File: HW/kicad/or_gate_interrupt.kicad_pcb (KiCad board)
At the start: 2 copper layers, 8 parts, among them P1 CONN_01X06, P2 CONN_01X03, U1 74LS32, U2 74HC02

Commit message: Added a few parts.
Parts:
- added P3: CONN_01X02, Pin_Headers:Pin_Header_Straight_1x02, F.Cu at (130.8, 120.7)
- added U3: ESP-01v090, ESP8266:ESP-01, F.Cu at (121.9, 96.5)
- P2: value CONN_01X03 -> CONN_01X02
- moved R2 7.41 mm to (114.3, 113.0)
- moved P2 7.18 mm to (114.3, 120.7)
- moved P1 5.68 mm to (114.3, 96.5), turned to 180 degrees
- moved R1 5.68 mm to (114.3, 102.9)
- moved R4 3.59 mm to (132.1, 102.9)
- moved U2 2.84 mm to (123.2, 111.8)
- moved R3 2.54 mm to (132.1, 113.0)
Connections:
- P2 pad 1: Net-(P2-Pad1) -> GND
- P2 pad 3: Net-(P1-Pad5) -> (no net)
- R1 pad 2: Net-(P2-Pad1) -> Net-(P2-Pad2)
- U1 pad 1: Net-(P2-Pad1) -> Net-(P2-Pad2)
- U2 pad 1: Net-(P2-Pad2) -> Net-(U2-Pad1)

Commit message: Updated a few layout things.
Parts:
- added C1: CP, Capacitors_ThroughHole:C_Radial_D6.3_L11.2_P2.5, F.Cu at (118.1, 94.0)
- added U4: LT1129CST-3.3, SOT-223, F.Cu at (116.8, 85.1)
- P2: footprint Pin_Headers:Pin_Header_Straight_1x03 -> Pin_Headers:Pin_Header_Straight_1x02
- moved P3 48.4 mm to (119.4, 73.7), turned to 0 degrees
- moved P2 44.5 mm to (114.3, 76.2), turned to 180 degrees
- moved P1 20.9 mm to (134.6, 101.6), turned to 0 degrees
- moved U3 4.02 mm to (125.7, 95.2)
- moved R3 2.54 mm to (129.5, 113.0)
- moved R4 2.54 mm to (129.5, 102.9)
- moved U2 1.80 mm to (121.9, 113.0)
- moved U1 1.27 mm to (121.9, 102.9)
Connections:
- P1 pad 6: +3V3 -> Net-(P1-Pad6)

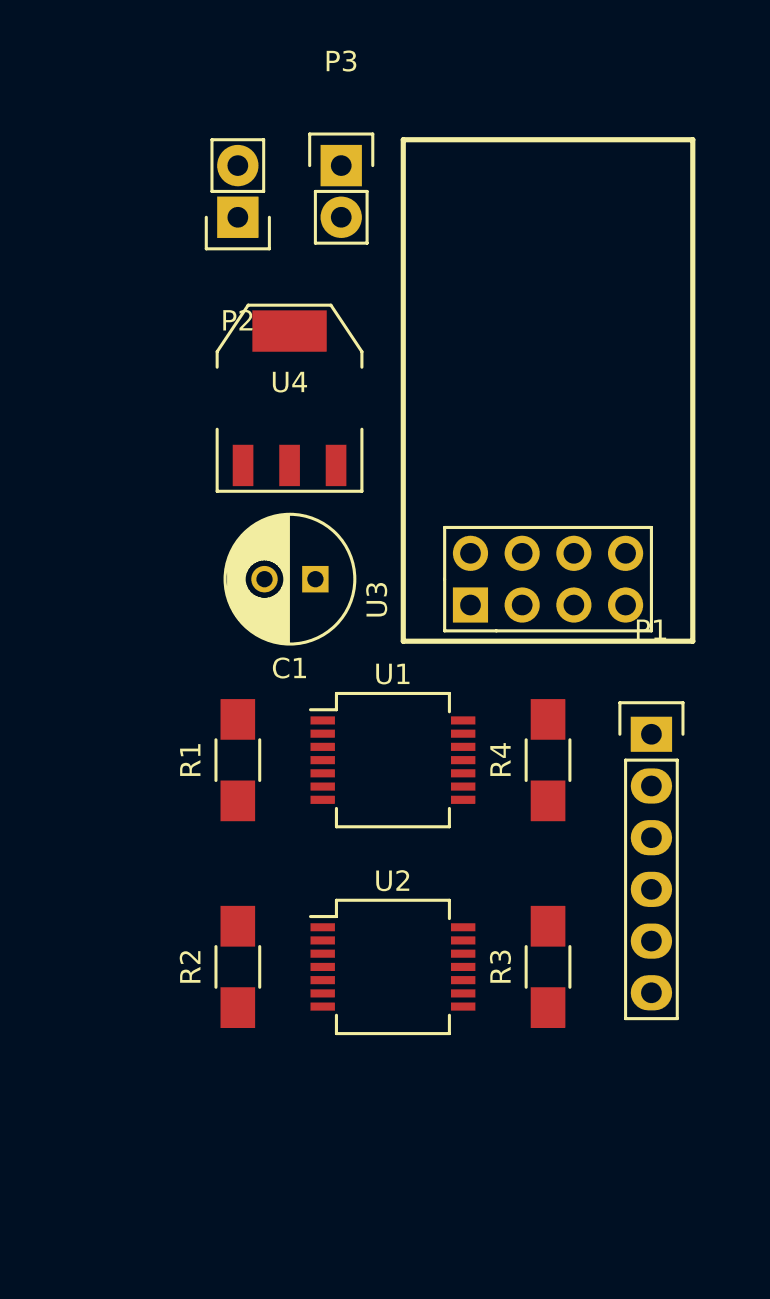
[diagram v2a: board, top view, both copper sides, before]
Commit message: Most of the routing done.  Trying to figure out ground plane.
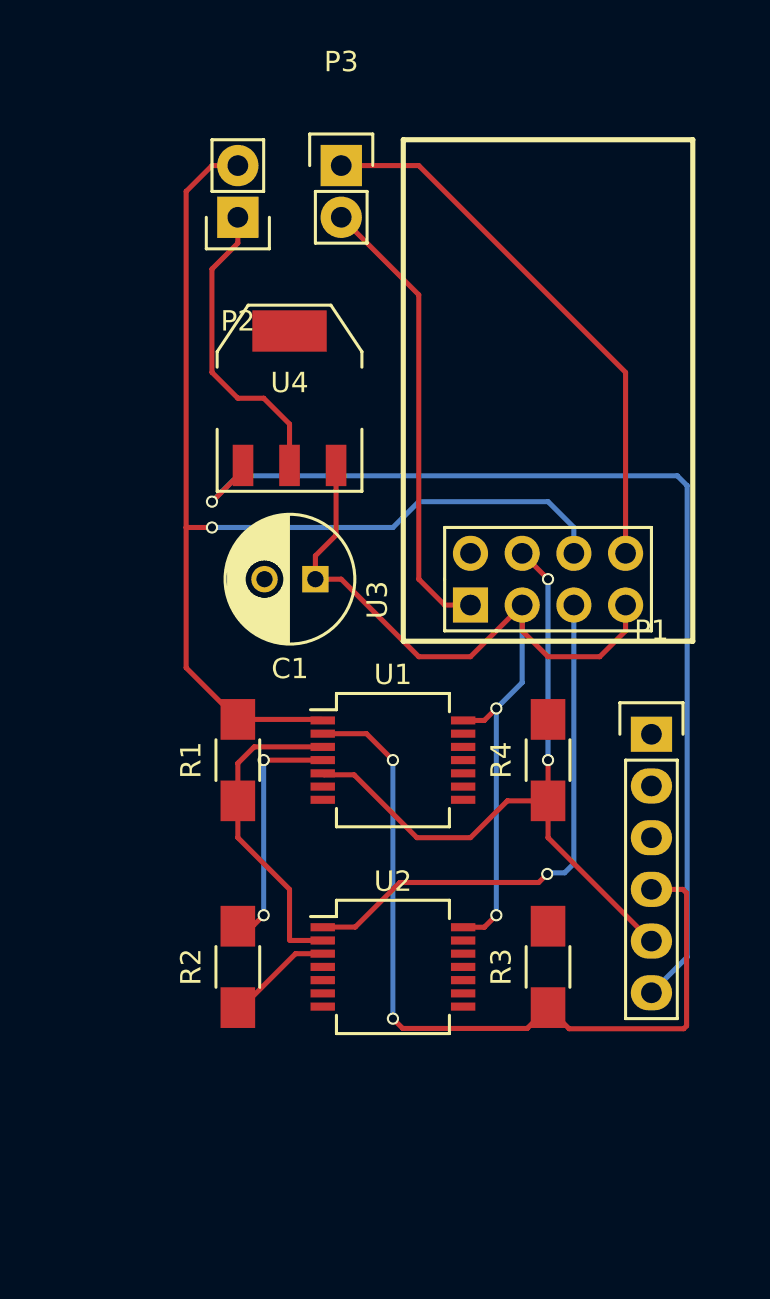
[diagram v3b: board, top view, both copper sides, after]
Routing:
- net Net-(P2-Pad2): track 0.00 -> 55.6 mm, vias 0 -> 2
- net Net-(P1-Pad6): track 0.00 -> 52.1 mm, vias 0 -> 1
- net +3V3: track 0.00 -> 47.0 mm, vias 0 -> 2
- net Net-(P1-Pad4): track 0.00 -> 40.6 mm, vias 0 -> 2
- net Net-(P1-Pad5): track 0.00 -> 34.8 mm, vias 0 -> 2
- net Net-(P3-Pad1): track 0.00 -> 27.1 mm
- net Net-(U2-Pad1): track 0.00 -> 26.3 mm, vias 0 -> 2
- net Net-(P3-Pad2): track 0.00 -> 22.4 mm
- net Net-(R1-Pad1): track 0.00 -> 15.9 mm
- net GND: track 0.00 -> 15.0 mm
- net Net-(R2-Pad2): track 0.00 -> 12.0 mm, vias 0 -> 2
- net Net-(R2-Pad1): track 0.00 -> 5.27 mm

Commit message: Think layout is done for first pass.
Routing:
- net GND: track 15.0 -> 44.5 mm, vias 0 -> 5
- net Net-(R2-Pad1): track 5.27 -> 20.8 mm, vias 0 -> 2
- added copper zone on B.Cu, net GND
- added copper zone on F.Cu, net GND
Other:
- board outline added: 27.9 x 47 mm

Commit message: Updated BOM.  Changed cap to smt.
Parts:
- C1: value CP -> 100uF; footprint Capacitors_ThroughHole:C_Radial_D6.3_L11.2_P2.5 -> Capacitors_SMD:C_1206_HandSoldering
- R1, R2, R3, R4: value R -> 1K
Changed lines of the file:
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@@
-(kicad_pcb (version 4) (host pcbnew 4.0.4-stable)
+(kicad_pcb (version 4) (host pcbnew 4.0.2+dfsg1-2~bpo8+1-stable)
   (general
     (links 32)
     (no_connects 0)
-    (area 110.489499 71.119499 138.430501 118.305)
+    (area 110.461667 71.119499 138.430501 118.205)
     (thickness 1.6)
     (drawings 4)
@@
       (effects (font (size 1 1) (thickness 0.15)))
     )
-    (fp_text value R (at 0 2.3 90) (layer F.Fab)
+    (fp_text value 1K (at 0 2.3 90) (layer F.Fab)
       (effects (font (size 1 1) (thickness 0.15)))
     )
@@
       (effects (font (size 1 1) (thickness 0.15)))
     )
-    (fp_text value R (at 0 2.3 90) (layer F.Fab)
+    (fp_text value 1K (at 0 2.3 90) (layer F.Fab)
       (effects (font (size 1 1) (thickness 0.15)))
     )
@@
       (effects (font (size 1 1) (thickness 0.15)))
     )
-    (fp_text value R (at 0 2.3 90) (layer F.Fab)
+    (fp_text value 1K (at 0 2.3 90) (layer F.Fab)
       (effects (font (size 1 1) (thickness 0.15)))
     )
@@
       (effects (font (size 1 1) (thickness 0.15)))
     )
-    (fp_text value R (at 0 2.3 90) (layer F.Fab)
+    (fp_text value 1K (at 0 2.3 90) (layer F.Fab)
       (effects (font (size 1 1) (thickness 0.15)))
     )
@@
     )
   )
-  (module Capacitors_ThroughHole:C_Radial_D6.3_L11.2_P2.5 (layer F.Cu)
-    (at 118.11 93.98 180)
-    (descr "Radial Electrolytic Capacitor, Diameter 6.3mm x Length 11.2mm, Pitch 2.5mm")
-    (tags "Electrolytic Capacitor")
-    (fp_text reference C1 (at 1.25 -4.4 180) (layer F.SilkS)
-      (effects (font (size 1 1) (thickness 0.15)))
-    )
-    (fp_text value CP (at 1.25 4.4 180) (layer F.Fab)
-      (effects (font (size 1 1) (thickness 0.15)))
-    )
-    (fp_line (start 1.325 -3.149) (end 1.325 3.149) (layer F.SilkS) (width 0.15))
-    (fp_line (start 1.465 -3.143) (end 1.465 3.143) (layer F.SilkS) (width 0.15))
-    (fp_line (start 1.605 -3.13) (end 1.605 -0.446) (layer F.SilkS) (width 0.15))
-    (fp_line (start 1.605 0.446) (end 1.605 3.13) (layer F.SilkS) (width 0.15))
-    (fp_line (start 1.745 -3.111) (end 1.745 -0.656) (layer F.SilkS) (width 0.15))
-    (fp_line (start 1.745 0.656) (end 1.745 3.111) (layer F.SilkS) (width 0.15))
-    (fp_line (start 1.885 -3.085) (end 1.885 -0.789) (layer F.SilkS) (width 0.15))
-    (fp_line (start 1.885 0.789) (end 1.885 3.085) (layer F.SilkS) (width 0.15))
-    (fp_line (start 2.025 -3.053) (end 2.025 -0.88) (layer F.SilkS) (width 0.15))
-    (fp_line (start 2.025 0.88) (end 2.025 3.053) (layer F.SilkS) (width 0.15))
-    (fp_line (start 2.165 -3.014) (end 2.165 -0.942) (layer F.SilkS) (width 0.15))
-    (fp_line (start 2.165 0.942) (end 2.165 3.014) (layer F.SilkS) (width 0.15))
-    (fp_line (start 2.305 -2.968) (end 2.305 -0.981) (layer F.SilkS) (width 0.15))
-    (fp_line (start 2.305 0.981) (end 2.305 2.968) (layer F.SilkS) (width 0.15))
-    (fp_line (start 2.445 -2.915) (end 2.445 -0.998) (layer F.SilkS) (width 0.15))
-    (fp_line (start 2.445 0.998) (end 2.445 2.915) (layer F.SilkS) (width 0.15))
-    (fp_line (start 2.585 -2.853) (end 2.585 -0.996) (layer F.SilkS) (width 0.15))
-    (fp_line (start 2.585 0.996) (end 2.585 2.853) (layer F.SilkS) (width 0.15))
-    (fp_line (start 2.725 -2.783) (end 2.725 -0.974) (layer F.SilkS) (width 0.15))
-    (fp_line (start 2.725 0.974) (end 2.725 2.783) (layer F.SilkS) (width 0.15))
-    (fp_line (start 2.865 -2.704) (end 2.865 -0.931) (layer F.SilkS) (width 0.15))
-    (fp_line (start 2.865 0.931) (end 2.865 2.704) (layer F.SilkS) (width 0.15))
-    (fp_line (start 3.005 -2.616) (end 3.005 -0.863) (layer F.SilkS) (width 0.15))
-    (fp_line (start 3.005 0.863) (end 3.005 2.616) (layer F.SilkS) (width 0.15))
-    (fp_line (start 3.145 -2.516) (end 3.145 -0.764) (layer F.SilkS) (width 0.15))
-    (fp_line (start 3.145 0.764) (end 3.145 2.516) (layer F.SilkS) (width 0.15))
-    (fp_line (start 3.285 -2.404) (end 3.285 -0.619) (layer F.SilkS) (width 0.15))
-    (fp_line (start 3.285 0.619) (end 3.285 2.404) (layer F.SilkS) (width 0.15))
-    (fp_line (start 3.425 -2.279) (end 3.425 -0.38) (layer F.SilkS) (width 0.15))
-    (fp_line (start 3.425 0.38) (end 3.425 2.279) (layer F.SilkS) (width 0.15))
-    (fp_line (start 3.565 -2.136) (end 3.565 2.136) (layer F.SilkS) (width 0.15))
-    (fp_line (start 3.705 -1.974) (end 3.705 1.974) (layer F.SilkS) (width 0.15))
-    (fp_line (start 3.845 -1.786) (end 3.845 1.786) (layer F.SilkS) (width 0.15))
-    (fp_line (start 3.985 -1.563) (end 3.985 1.563) (layer F.SilkS) (width 0.15))
-    (fp_line (start 4.125 -1.287) (end 4.125 1.287) (layer F.SilkS) (width 0.15))
-    (fp_line (start 4.265 -0.912) (end 4.265 0.912) (layer F.SilkS) (width 0.15))
-    (fp_circle (center 2.5 0) (end 2.5 -1) (layer F.SilkS) (width 0.15))
-    (fp_circle (center 1.25 0) (end 1.25 -3.1875) (layer F.SilkS) (width 0.15))
-    (fp_circle (center 1.25 0) (end 1.25 -3.4) (layer F.CrtYd) (width 0.05))
-    (pad 2 thru_hole circle (at 2.5 0 180) (size 1.3 1.3) (drill 0.8) (layers *.Cu *.Mask F.SilkS)
-      (net 1 GND))
-    (pad 1 thru_hole rect (at 0 0 180) (size 1.3 1.3) (drill 0.8) (layers *.Cu *.Mask F.SilkS)
-      (net 4 +3V3))
-    (model Capacitors_ThroughHole.3dshapes/C_Radial_D6.3_L11.2_P2.5.wrl
-      (at (xyz 0 0 0))
-      (scale (xyz 1 1 1))
-      (rotate (xyz 0 0 0))
-    )
-  )
   (module Pin_Headers:Pin_Header_Straight_1x02 (layer F.Cu)
     (at 114.3 76.2 180)
@@
     )
   )
+  (module Capacitors_SMD:C_1206_HandSoldering (layer F.Cu)
+    (at 118.11 93.98 180)
+    (descr "Capacitor SMD 1206, hand soldering")
+    (tags "capacitor 1206")
+    (attr smd)
+    (fp_text reference C1 (at 0 -2.3 180) (layer F.SilkS)
+      (effects (font (size 1 1) (thickness 0.15)))
+    )
+    (fp_text value 100uF (at 0 2.3 180) (layer F.Fab)
+      (effects (font (size 1 1) (thickness 0.15)))
+    )
+    (fp_line (start -3.3 -1.15) (end 3.3 -1.15) (layer F.CrtYd) (width 0.05))
+    (fp_line (start -3.3 1.15) (end 3.3 1.15) (layer F.CrtYd) (width 0.05))
+    (fp_line (start -3.3 -1.15) (end -3.3 1.15) (layer F.CrtYd) (width 0.05))
+    (fp_line (start 3.3 -1.15) (end 3.3 1.15) (layer F.CrtYd) (width 0.05))
+    (fp_line (start 1 -1.025) (end -1 -1.025) (layer F.SilkS) (width 0.15))
+    (fp_line (start -1 1.025) (end 1 1.025) (layer F.SilkS) (width 0.15))
+    (pad 1 smd rect (at -2 0 180) (size 2 1.6) (layers F.Cu F.Paste F.Mask)
+      (net 4 +3V3))
+    (pad 2 smd rect (at 2 0 180) (size 2 1.6) (layers F.Cu F.Paste F.Mask)
+      (net 1 GND))
+    (model Capacitors_SMD.3dshapes/C_1206_HandSoldering.wrl
+      (at (xyz 0 0 0))
+      (scale (xyz 1 1 1))
+      (rotate (xyz 0 0 0))
+    )
+  )

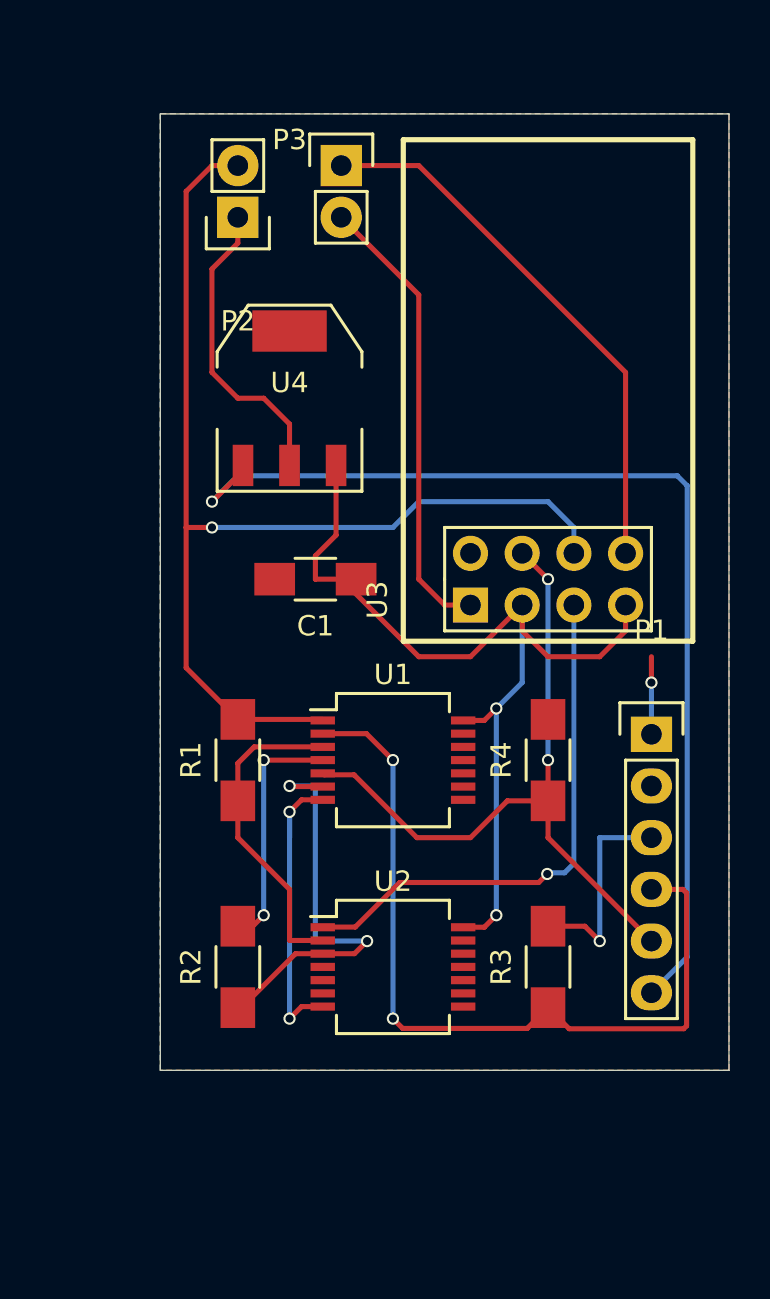
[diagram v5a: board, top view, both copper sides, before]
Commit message: Rerouted with new resistor size.  Need to shrink board.
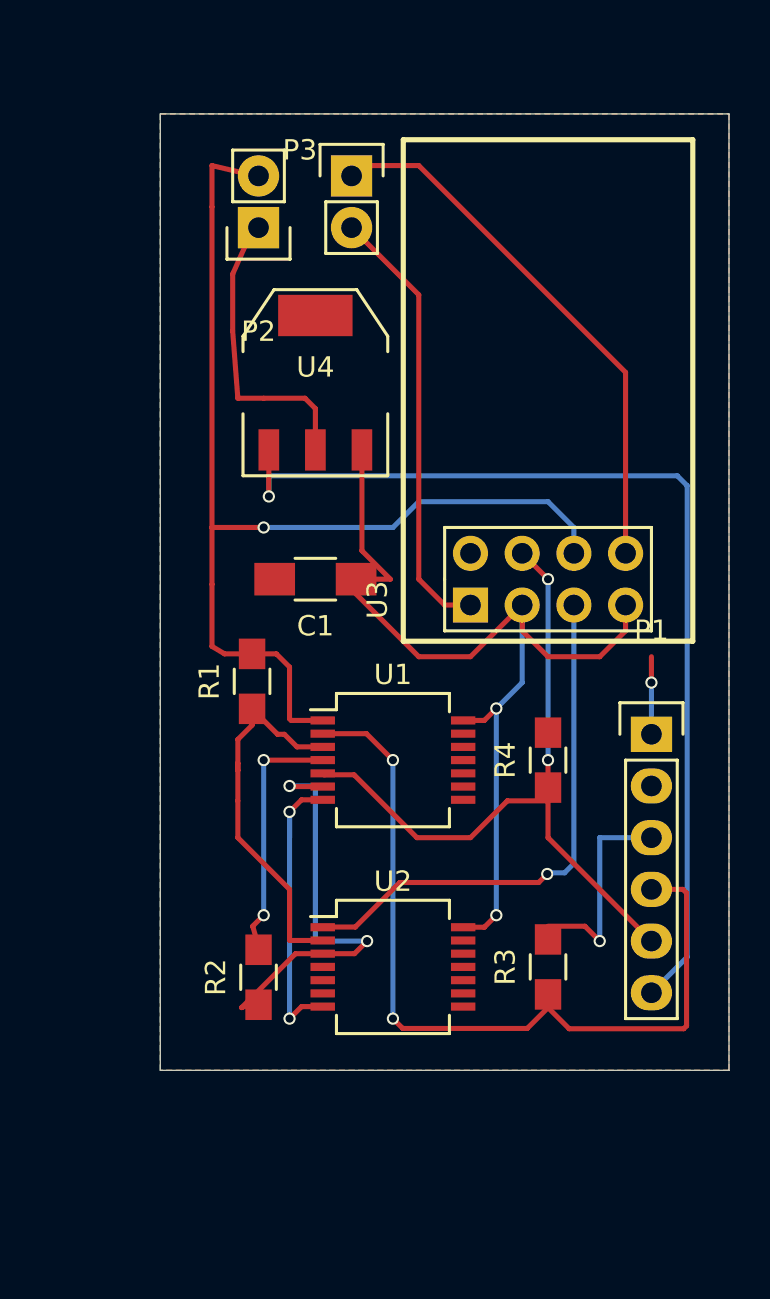
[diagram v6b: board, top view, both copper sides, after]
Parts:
- P1: value CONN_01X06 -> V_I1_I2_G_G_G
- P3: value CONN_01X02 -> Rx_Tx
- R1, R2, R3, R4: footprint Resistors_SMD:R_1206_HandSoldering -> Resistors_SMD:R_0805_HandSoldering
- moved R1 3.93 mm to (115.0, 99.0)
- moved U4 1.48 mm to (118.1, 84.3)
- moved P2 1.14 mm to (115.3, 76.7)
- moved R2 1.14 mm to (115.3, 113.5)
- moved P3 0.72 mm to (119.9, 74.2)
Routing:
- net Net-(R1-Pad1): track 15.9 -> 18.9 mm
- net Net-(P1-Pad6): track 52.1 -> 49.7 mm
- net +3V3: track 47.0 -> 48.3 mm
- net Net-(P2-Pad2): track 55.6 -> 54.4 mm
